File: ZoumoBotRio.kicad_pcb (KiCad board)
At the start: 2 copper layers, 83.2 x 52.1 mm, 148 parts, among them CON1 BARREL_JACK, J1 Screw_Terminal_1x05, J2 Screw_Terminal_1x05, P1 USB_OTG, P10 Analog, P11 Digital, P12 Analog, P13 Digital, P14 CONN_01X06, P2 Analog, P3 Digital, P4 Analog, P5 Digital, P6 Analog, P7 Digital, P8 Analog, P9 Digital, Q1 Q_PMOS_GDS, Q2 IR Receiver, Q3 IR Receiver, U1 ZLDO1117K50TC, U2 ATmega32U4-AU, U3 SOT361-1_2, U4 TB6612FNG, U5 TB6612FNG, Y1 16MHz

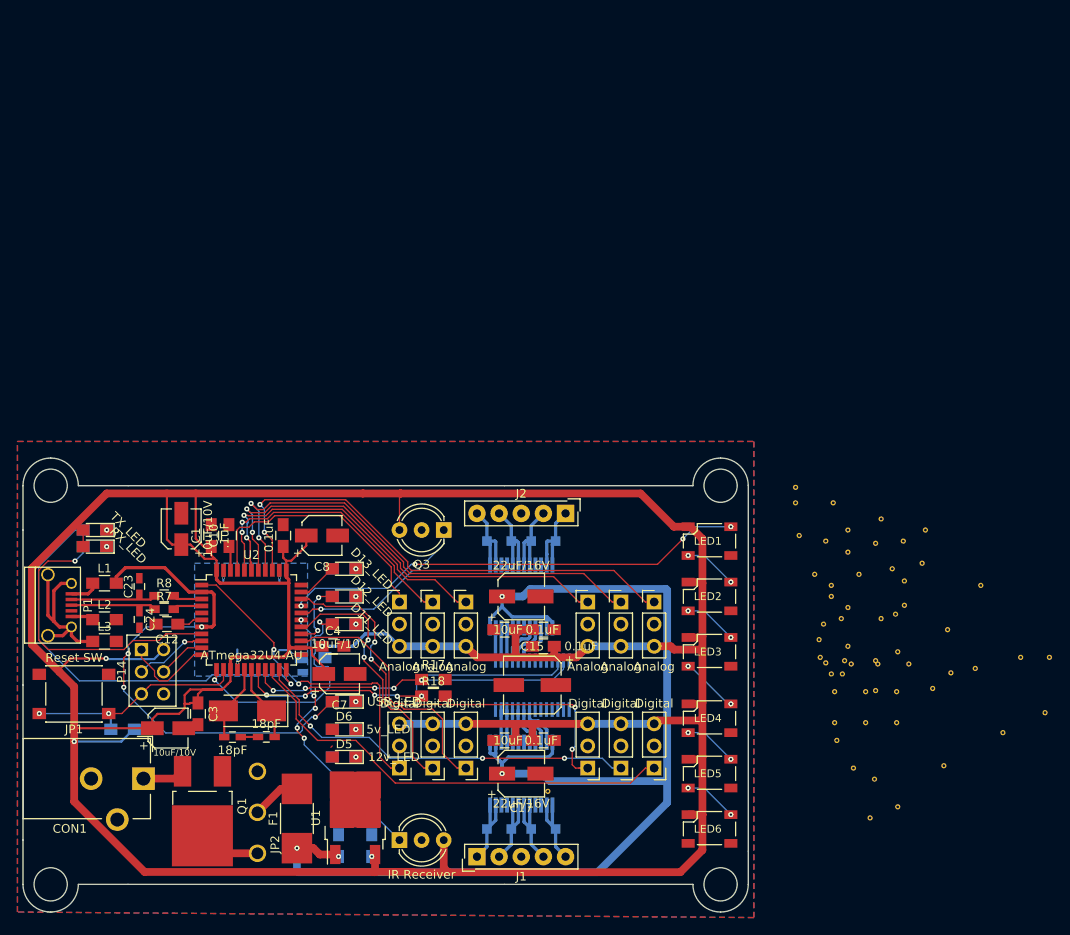
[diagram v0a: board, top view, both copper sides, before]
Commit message: Minor modifications to PCB, uploaded correct schematic
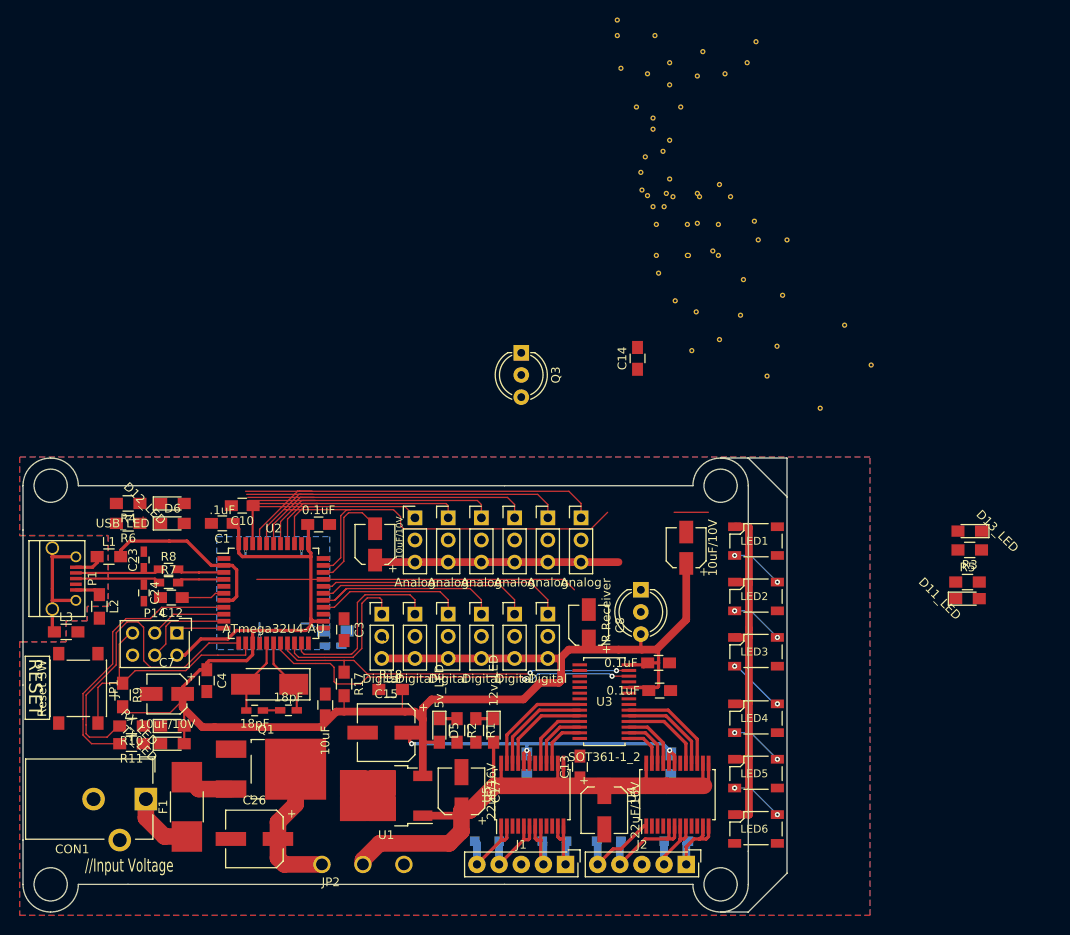
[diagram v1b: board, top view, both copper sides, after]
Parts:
- added C26: C, Capacitors_SMD:CP_Elec_6.3x7.7, F.Cu at (130.7, 129.4)
- C13, C14, R1, R10, R11, R2, R3, R4, R5, R6, R9, U3, U4, U5: moved to F.Cu
- C19, C22: moved to B.Cu
- moved REF** 89.2 mm to (188.2, 38.0)
- moved D2 71.9 mm to (212.7, 94.1)
- moved R3 71.8 mm to (212.7, 96.3)
- moved R5 71.7 mm to (212.5, 99.9), turned to 0 degrees
- moved D4 71.6 mm to (212.5, 101.9), turned to 0 degrees
- moved C14 63.7 mm to (174.6, 74.3)
- moved REF** 60.3 mm to (186.8, 65.3)
- moved REF** 58.6 mm to (145.7, 106.6)
- moved C6 58.0 mm to (180.2, 96.0)
- moved REF** 57.4 mm to (181.5, 41.9)
- moved REF** 57.4 mm to (184.0, 72.1)
- moved REF** 57.4 mm to (181.4, 69.0)
- moved REF** 57.4 mm to (176.8, 58.9)
- moved REF** 57.4 mm to (180.3, 58.9)
- moved REF** 57.4 mm to (183.9, 58.9)
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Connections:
- F1 pad 1: +12V -> Net-(CON1-Pad1)
- JP2 pad 2: Net-(F1-Pad2) -> +12V
- Q1 pad 3: Net-(CON1-Pad1) -> Net-(F1-Pad2)
- U2 pad 1: D7 -> Net-(U2-Pad1)
- U2 pad 12: D11 -> Net-(R10-Pad2)
- U2 pad 22: Net-(R11-Pad2) -> Net-(U2-Pad22)
- U2 pad 25: D4 -> Net-(U2-Pad25)
- U2 pad 26: D12 -> D4
- U2 pad 27: D6 -> D5
- U2 pad 28: D8 -> D6
- U2 pad 29: D9 -> D7
- U2 pad 30: D10 -> D8
- U2 pad 31: D5 -> D9
- U2 pad 32: D13 -> D10
- U2 pad 36: A0 -> A5
- U2 pad 37: A1 -> A4
- U2 pad 38: A2 -> A3
- U2 pad 39: A3 -> A2
- U2 pad 40: A4 -> A1
- U2 pad 41: A5 -> A0
- U2 pad 8: Net-(R10-Pad2) -> Net-(R11-Pad2)
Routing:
- net +5V: track 450.9 -> 306.0 mm, vias 4 -> 3
- net (no net): track 0.23 -> 80.2 mm
- net +12V: track 145.0 -> 70.6 mm, vias 4 -> 0
- net /AREF: track 2.53 -> 71.6 mm
- net D10: track 53.3 -> 8.63 mm, vias 4 -> 0
- net UVcc: track 61.1 -> 20.6 mm, vias 4 -> 0
- net D0/RXI: track 51.8 -> 19.0 mm
- net D8: track 31.8 -> 0.00 mm, vias 5 -> 0
- net A3: track 40.6 -> 9.04 mm, vias 2 -> 0
- net D4: track 46.6 -> 17.1 mm, vias 2 -> 0
- net D11: track 27.7 -> 0.00 mm, vias 2 -> 0
- net A4: track 32.7 -> 8.52 mm, vias 2 -> 0
- net D1/TXO: track 45.6 -> 21.9 mm, vias 3 -> 0
- net A5: track 29.8 -> 8.02 mm
- net D9: track 21.2 -> 1.79 mm, vias 1 -> 0
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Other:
- board size 83.2 x 52.1 mm -> 87.6 x 52.1 mm
- board text added: "//Input Voltage"
- board text added: "RESET"
